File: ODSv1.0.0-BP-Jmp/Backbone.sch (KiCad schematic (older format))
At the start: 32 parts, among them J1 Conn_01x16

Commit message: Define a no-IC variant of BP-Jmp
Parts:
- D4, D5, D6, D7, D8, R19, R20, R21, R22, R23: Config (none) -> -NoIC
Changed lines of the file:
@@
 F 7 "SMD" H 9000 4550 50  0001 C CNN "Type"
 F 8 "311-560HRCT-ND" H 9000 4550 50  0001 C CNN "Digikey ID"
+F 9 "-NoIC" H 9000 4550 50  0001 C CNN "Config"
 	1    9000 4550
 	0    1    1    0
@@
 F 7 "SMD" H 9000 4650 50  0001 C CNN "Type"
 F 8 "311-560HRCT-ND" H 9000 4650 50  0001 C CNN "Digikey ID"
+F 9 "-NoIC" H 9000 4650 50  0001 C CNN "Config"
 	1    9000 4650
 	0    1    1    0
@@
 F 7 "SMD" H 9000 4750 50  0001 C CNN "Type"
 F 8 "311-560HRCT-ND" H 9000 4750 50  0001 C CNN "Digikey ID"
+F 9 "-NoIC" H 9000 4750 50  0001 C CNN "Config"
 	1    9000 4750
 	0    1    1    0
@@
 F 7 "SMD" H 9000 4850 50  0001 C CNN "Type"
 F 8 "311-560HRCT-ND" H 9000 4850 50  0001 C CNN "Digikey ID"
+F 9 "-NoIC" H 9000 4850 50  0001 C CNN "Config"
 	1    9000 4850
 	0    1    1    0
@@
 F 7 "SMD" H 9000 4950 50  0001 C CNN "Type"
 F 8 "311-560HRCT-ND" H 9000 4950 50  0001 C CNN "Digikey ID"
+F 9 "-NoIC" H 9000 4950 50  0001 C CNN "Config"
 	1    9000 4950
 	0    1    1    0
@@
 F 8 "Polarity is indicated by a diode symbol either next to the LED or at the end of the line of LEDs." H 8550 4950 50  0001 C CNN "Assembly Notes"
 F 9 "160-1437-1-ND" H 8550 4950 50  0001 C CNN "Digikey ID"
+F 10 "-NoIC" H 8550 4950 50  0001 C CNN "Config"
 	1    8550 4950
 	1    0    0    1
@@
 F 8 "Polarity is indicated by a diode symbol either next to the LED or at the end of the line of LEDs." H 8550 4850 50  0001 C CNN "Assembly Notes"
 F 9 "160-1437-1-ND" H 8550 4850 50  0001 C CNN "Digikey ID"
+F 10 "-NoIC" H 8550 4850 50  0001 C CNN "Config"
 	1    8550 4850
 	1    0    0    1
@@
 F 8 "Polarity is indicated by a diode symbol either next to the LED or at the end of the line of LEDs." H 8550 4750 50  0001 C CNN "Assembly Notes"
 F 9 "160-1437-1-ND" H 8550 4750 50  0001 C CNN "Digikey ID"
+F 10 "-NoIC" H 8550 4750 50  0001 C CNN "Config"
 	1    8550 4750
 	1    0    0    1
@@
 F 8 "Polarity is indicated by a diode symbol either next to the LED or at the end of the line of LEDs." H 8550 4650 50  0001 C CNN "Assembly Notes"
 F 9 "160-1437-1-ND" H 8550 4650 50  0001 C CNN "Digikey ID"
+F 10 "-NoIC" H 8550 4650 50  0001 C CNN "Config"
 	1    8550 4650
 	1    0    0    1
@@
 F 8 "Polarity is indicated by a diode symbol either next to the LED or at the end of the line of LEDs." H 8550 4550 50  0001 C CNN "Assembly Notes"
 F 9 "160-1437-1-ND" H 8550 4550 50  0001 C CNN "Digikey ID"
+F 10 "-NoIC" H 8550 4550 50  0001 C CNN "Config"
 	1    8550 4550
 	1    0    0    1

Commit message: Make minor improvements to PP-T41 (#20)
* Fix 3D models for Teensy 4.1 and female headers to mount it (#18)

* Add header as test points for signal not exposed on the backbone (#15)
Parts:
- J1: Manufacturer Sullins Connector Solutions -> Sullins
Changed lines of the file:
@@
 F 4 "S1113E-16-ND" H 4800 5050 50  0001 C CNN "Digikey ID"
 F 5 "GEC16SBSN-M89" H 4800 5050 50  0001 C CNN "MPN"
-F 6 "Sullins Connector Solutions" H 4800 5050 50  0001 C CNN "Manufacturer"
+F 6 "Sullins" H 4800 5050 50  0001 C CNN "Manufacturer"
 F 7 "https://www.digikey.com/en/products/detail/sullins-connector-solutions/GEC16SBSN-M89/862267" H 4800 5050 50  0001 C CNN "Ordering URL"
 F 8 "SMD" H 4800 5050 50  0001 C CNN "Type"

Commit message: Change indicator LEDs and make them dimmer (#14)
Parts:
- D1, D2, D3: value Blue -> Green; Digikey ID 160-1646-1-ND -> 732-4971-1-ND; MPN LTST-C190TBKT -> 150060GS75000; Manufacturer Lite-On -> Wurth Elektronik; Ordering URL https://www.digikey.com/en/products/detail/lite-on-inc/LTST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 -> https://www.digikey.com/en/products/detail/w%C3%BCrth-elekt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
- D4, D5, D6, D7, D8: value Yellow -> Blue; Digikey ID 160-1437-1-ND -> 732-4966-1-ND; MPN LTST-C190KSKT -> 150060BS75000; Manufacturer Lite-On -> Wurth Elektronik; Ordering URL https://www.digikey.com/en/products/detail/lite-on-inc/LTST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 -> https://www.digikey.com/en/products/detail/w%C3%BCrth-elekt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
- R16: value 270 -> 7.5k; Digikey ID 311-270HRCT-ND -> 311-7.50KHRCT-ND; MPN RC0603FR-07270RL -> RC0603FR-077K5L; Ordering URL https://www.digikey.com/en/products/detail/yageo/RC0603FR-07270RL/727103 -> https://www.digikey.com/en/products/detail/yageo/RC0603FR-077K5L/727366
- R17: value 1k -> 7.5k; Digikey ID 311-1.00KHRCT-ND -> 311-7.50KHRCT-ND; MPN RC0603FR-071KL -> RC0603FR-077K5L; Ordering URL https://www.digikey.com/en/products/detail/yageo/RC0603FR-071KL/726843 -> https://www.digikey.com/en/products/detail/yageo/RC0603FR-077K5L/727366
- R18: value 1.2k -> 20k; Digikey ID 311-1.20KHRCT-ND -> 311-20.0KHRCT-ND; MPN RC0603FR-071K2L -> RC0603FR-0720KL; Ordering URL https://www.digikey.com/en/products/detail/yageo/RC0603FR-071K2L/726852 -> https://www.digikey.com/en/products/detail/yageo/RC0603FR-0720KL/727040
- R19, R20, R21, R22, R23: value 560 -> 2k; Digikey ID 311-560HRCT-ND -> 311-2.00KHRCT-ND; MPN RC0603FR-07560RL -> RC0603FR-072KL; Ordering URL https://www.digikey.com/en/products/detail/yageo/RC0603FR-07560RL/727304 -> https://www.digikey.com/en/products/detail/yageo/RC0603FR-072KL/727009

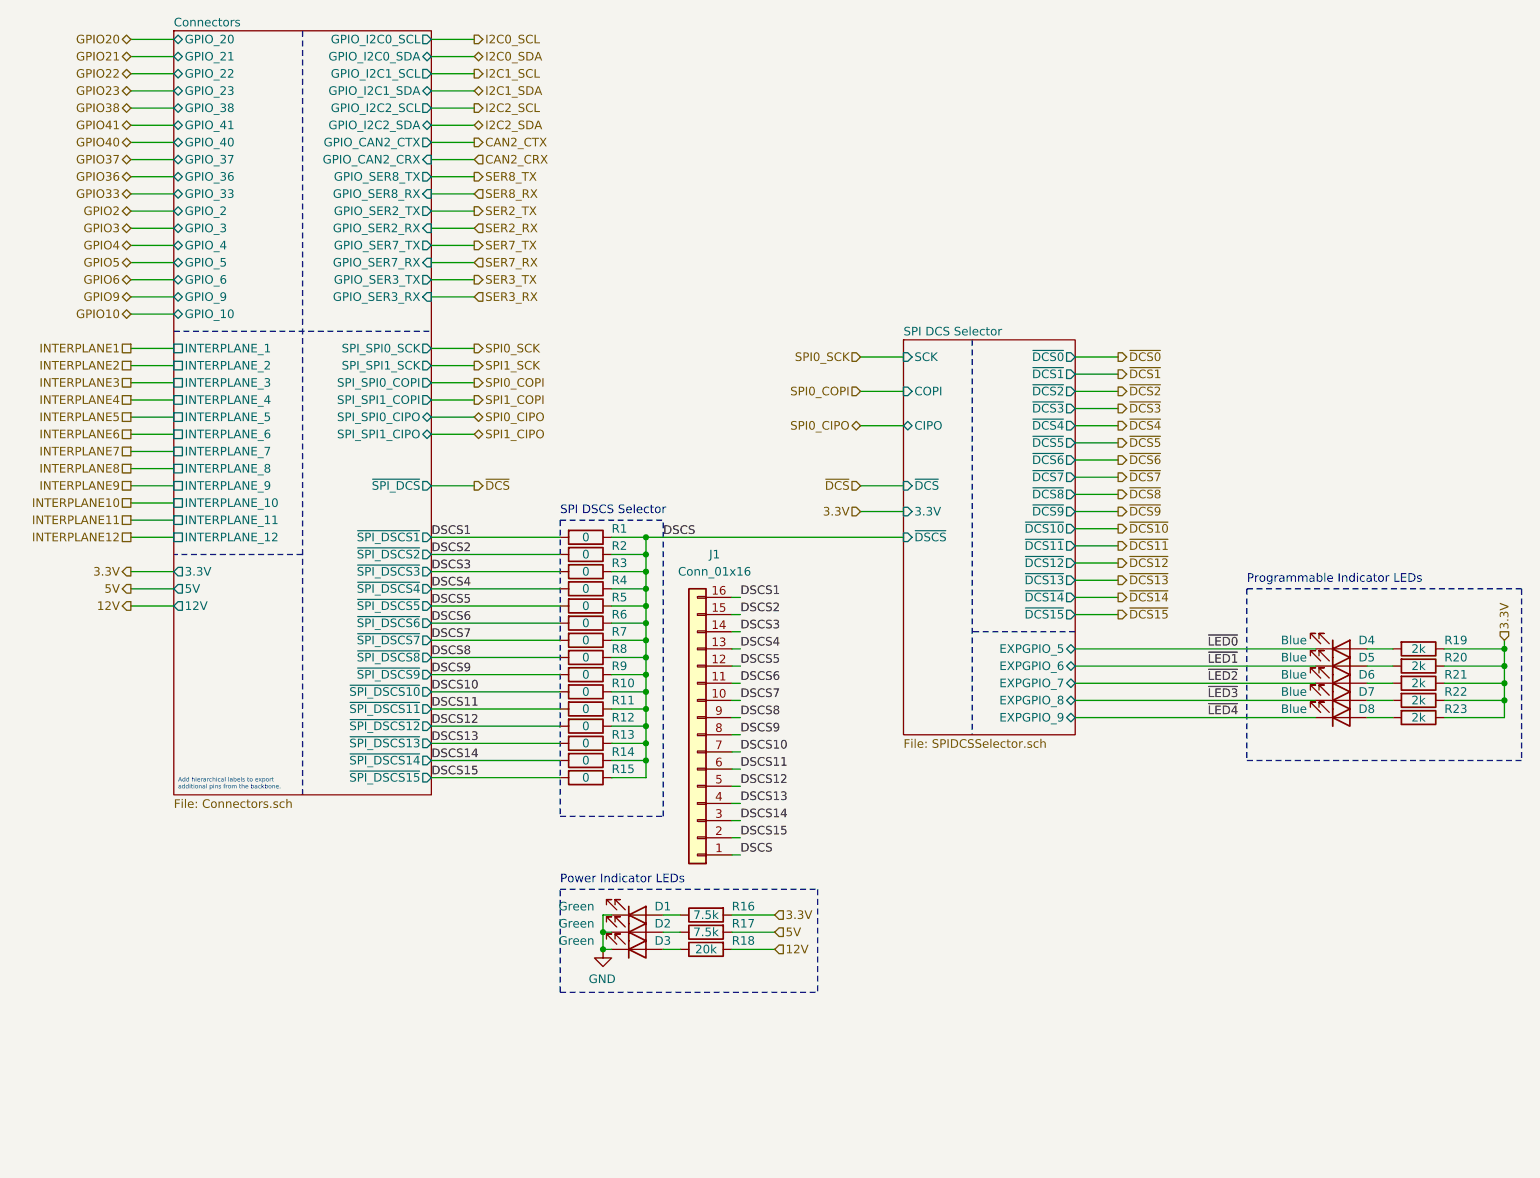
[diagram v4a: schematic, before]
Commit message: Fix implementation of SPI CS multiplexing system (#22)
* Disconnect PP-T41's MAX7317's DOUT, since it's not needed anyways (#16)

* Disconnect BT & BP-Jmp backbone MAX7317 DOUT (#16); make DOUT output pin

* Replace DAC with a second MAX7317 expander with pullup resistors

* Insert 3-state buffers between MAX7317 DOUTs and CIPO in BP-Jmp (#16)

* Update symbol fields for I/O expansion components in BP-Jmp

* Consolidate free space by moving the AD7689 chip

* Add pull-ups on demuxed DCS (#17), move pull-ups to bottom of BP-Jmp

* Insert 3-state buffers between all MAX7317 DOUTs and CIPO (#16)

* Add bypass caps to the 3-state buffers for BP-Jmp's I/O expanders

* Fix title block for SPI DCS Selector sheet in BP-Jmp

* Use 2k pullups instead of 20k pullups on BP-Jmp

* Add 2k pullups on demuxed DSCS pins in PP-T41

* Define a NoPufferfish BOM variant of PP-T41

* Adjust the 12V copper fills on PP-T41

* Add 2k pullups within the DSCS selector in PP-T41 (#17)

* Add more information to READMEs

* Add 2k pullups within DCS selectors (#17), bump BP-Jmp to 0.2.0

* Fix errors in PR template for modified boards

* Move usage on I/O peripherals into a subsection in BP-Jmp's README.md

* Update KiCad preview & mechanical renders of all boards

* Improve & consolidate pull request templates

* Update raytrace renders of the entire stack

* Add missing definition for NoPufferfish variant for PP-T41

* Add link to CADLab project for this repo

* Remove the message annoyingly added by CADLab to top of README.md
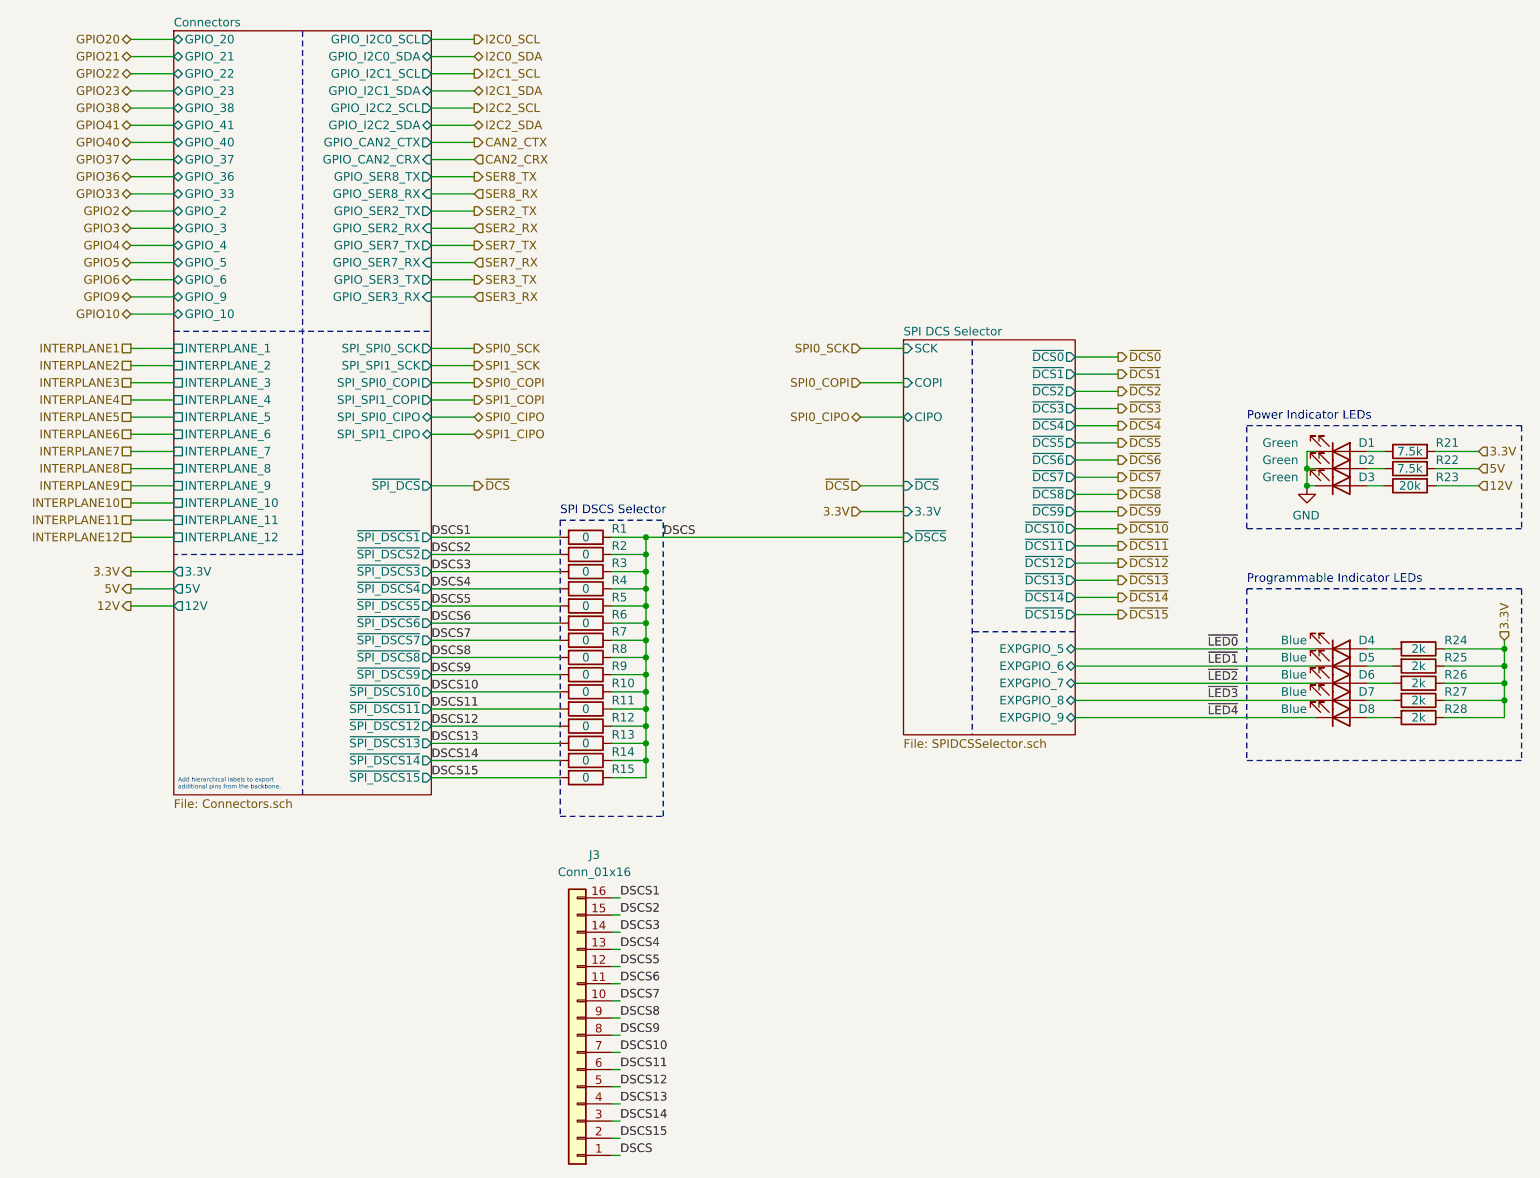
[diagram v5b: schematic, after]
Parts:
- J3: renamed from J1; Config (none) -> -NoIC
- R24: renamed from R19; Digikey ID 311-2.00KHRCT-ND -> 311-20.0KHRCT-ND; MPN RC0603FR-072KL -> RC0603FR-0720KL; Ordering URL https://www.digikey.com/en/products/detail/yageo/RC0603FR-072KL/727009 -> https://www.digikey.com/en/products/detail/yageo/RC0603FR-0720KL/727040
- R25: renamed from R20; Digikey ID 311-2.00KHRCT-ND -> 311-20.0KHRCT-ND; MPN RC0603FR-072KL -> RC0603FR-0720KL; Ordering URL https://www.digikey.com/en/products/detail/yageo/RC0603FR-072KL/727009 -> https://www.digikey.com/en/products/detail/yageo/RC0603FR-0720KL/727040
- R26: renamed from R21; Digikey ID 311-2.00KHRCT-ND -> 311-20.0KHRCT-ND; MPN RC0603FR-072KL -> RC0603FR-0720KL; Ordering URL https://www.digikey.com/en/products/detail/yageo/RC0603FR-072KL/727009 -> https://www.digikey.com/en/products/detail/yageo/RC0603FR-0720KL/727040
- R27: renamed from R22; Digikey ID 311-2.00KHRCT-ND -> 311-20.0KHRCT-ND; MPN RC0603FR-072KL -> RC0603FR-0720KL; Ordering URL https://www.digikey.com/en/products/detail/yageo/RC0603FR-072KL/727009 -> https://www.digikey.com/en/products/detail/yageo/RC0603FR-0720KL/727040
- R28: renamed from R23; Digikey ID 311-2.00KHRCT-ND -> 311-20.0KHRCT-ND; MPN RC0603FR-072KL -> RC0603FR-0720KL; Ordering URL https://www.digikey.com/en/products/detail/yageo/RC0603FR-072KL/727009 -> https://www.digikey.com/en/products/detail/yageo/RC0603FR-0720KL/727040
- renumbered R16 to R21, R17 to R22, R18 to R23
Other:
- moved on the sheet: D1, D2, D3, J3, R21, R22, R23
